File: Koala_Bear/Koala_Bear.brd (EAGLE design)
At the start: 59.3 x 40 mm, 27 parts

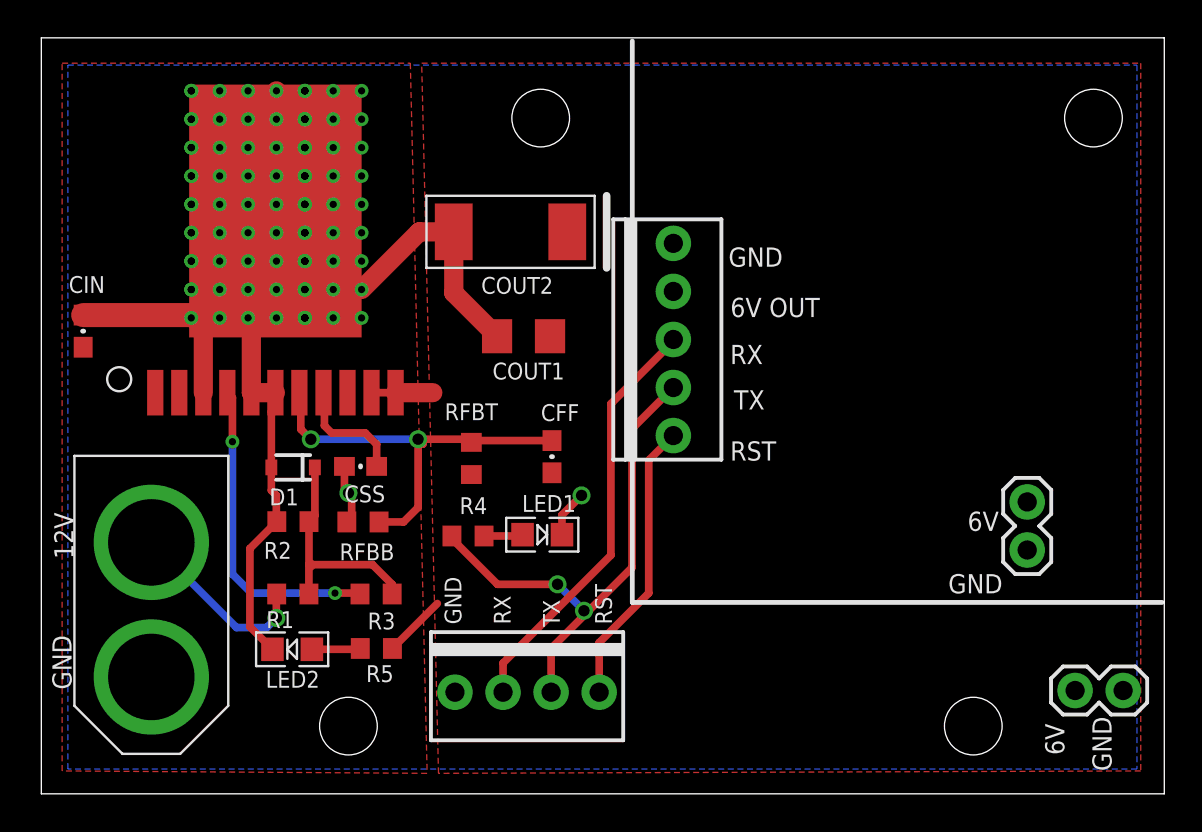
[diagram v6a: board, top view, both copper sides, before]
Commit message: Preliminary Rev C Koala
The only things that have changed since Rev B are power pin alignments
(lower right hand side), silkscreens, and power connector (the board has
now been Anderson-ified.) No changes have been made to the faulty TX LED
system; pending @douglashutchings et. al.s' go-ahead, I'll try a new fix
on that. I just wanted to get a pull request issued before the deadline.
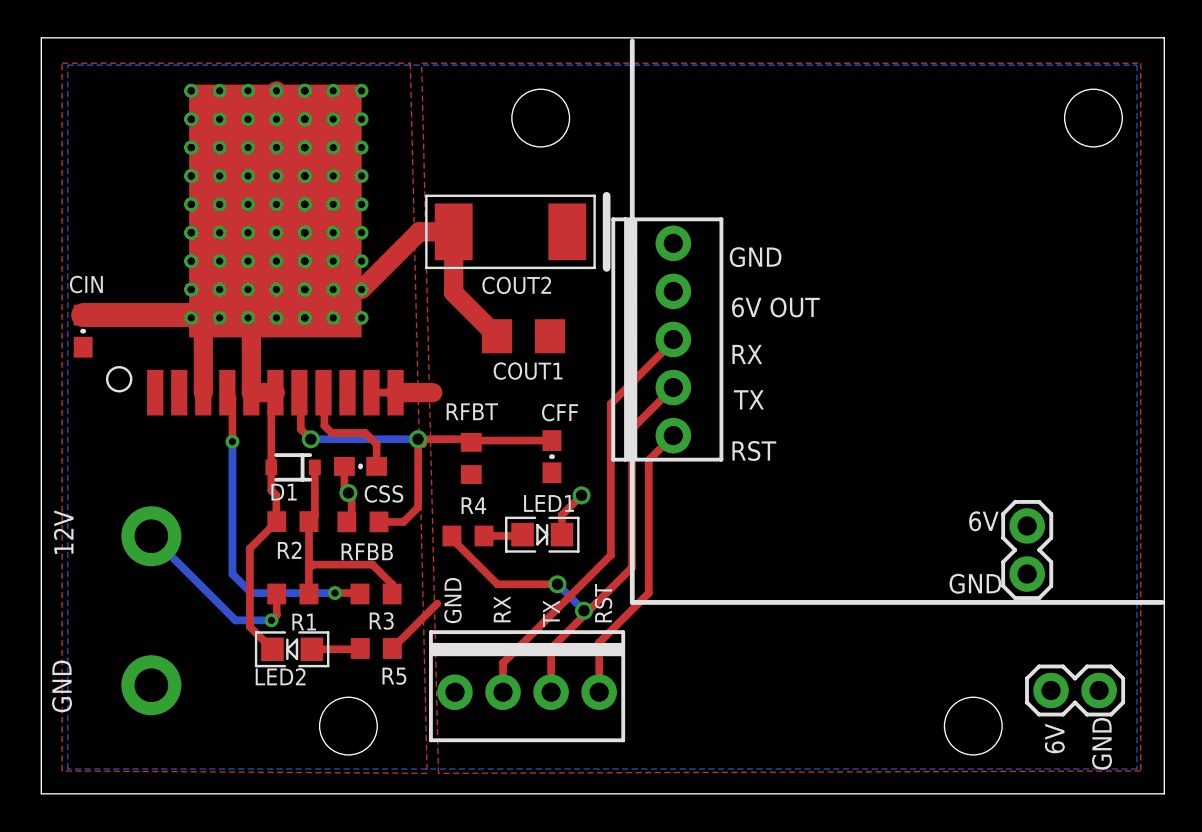
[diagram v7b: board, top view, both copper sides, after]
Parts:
- removed XT60: XT60CONNECTOR, pie_new:XT60CONNECTOR
- added U$6: ANDERSONVERTICAL, pie:ANDERSON_VERTICAL
- moved SERVO_PWR_6 1.27 mm to (60.0, 15.3)
- moved SERVO_PWR_12 1.27 mm to (62.5, 7.85)
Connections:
- net GND: now also U$6.PIN1; no longer XT60.GND
- net VIN: now also U$6.PIN2; no longer XT60.12V
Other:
- board text added: "Copyright (c) 2013, Pioneers in Engineering All rights reserved. Designed by: K. Rakelly and A. Hild This design is open source hardware. 12/21/2013"
- board text added: "PiE Robotics Buck Switching Regulator Version 2 : Revision C"
- board text removed: "Copyright (c) 2013, Pioneers in Engineering All rights reserved. Designed by: K. Rakelly and A. Hild This design is open source hardware. 11/13/2013"
- board text removed: "PiE Robotics Buck Switching Regulator Version 2 : Revision B"
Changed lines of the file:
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@@
 <setting verticaltext="up"/>
 </settings>
-<grid distance="0.005" unitdist="inch" unit="inch" style="lines" multiple="1" display="yes" altdistance="0.005" altunitdist="inch" altunit="inch"/>
+<grid distance="0.005" unitdist="inch" unit="inch" style="lines" multiple="1" display="yes" altdistance="0.1" altunitdist="inch" altunit="inch"/>
 <layers>
 <layer number="1" name="Top" color="4" fill="1" visible="yes" active="yes"/>
@@
 <layer number="97" name="Info" color="7" fill="1" visible="no" active="no"/>
 <layer number="98" name="Guide" color="6" fill="1" visible="no" active="no"/>
+<layer number="99" name="SpiceOrder" color="5" fill="1" visible="no" active="no"/>
 <layer number="100" name="Muster" color="7" fill="1" visible="no" active="no"/>
 <layer number="101" name="Patch_Top" color="12" fill="4" visible="no" active="yes"/>
@@
 <text x="57.758" y="19.658" size="1.016" layer="22" font="vector" ratio="15" rot="MR90">PiE Robotics
 Buck Switching Regulator
-Version 2 : Revision B</text>
+Version 2 : Revision C</text>
 <wire x1="67.244" y1="2.39" x2="7.9" y2="2.39" width="0" layer="20"/>
 <wire x1="39.13" y1="12.505" x2="39.13" y2="42.17291875" width="0.254" layer="25"/>
@@
 <text x="35.3" y="11.219" size="0.889" layer="21" font="vector" ratio="20" rot="R90">TX</text>
 <text x="32.7" y="11.346" size="0.889" layer="21" font="vector" ratio="20" rot="R90">RX</text>
-<text x="9.5" y="7.9" size="1.016" layer="21" font="vector" ratio="20" rot="R90">GND</text>
-<text x="9.6" y="14.8" size="1.016" layer="21" font="vector" ratio="20" rot="R90">12V</text>
+<text x="9.5" y="6.63" size="1.016" layer="21" font="vector" ratio="20" rot="R90">GND</text>
+<text x="9.6" y="14.927" size="1.016" layer="21" font="vector" ratio="20" rot="R90">12V</text>
 <text x="58.7" y="14" size="1.016" layer="21" font="vector" ratio="20" rot="R180">GND</text>
 <text x="58.5" y="17.3" size="1.016" layer="21" font="vector" ratio="20" rot="R180">6V</text>
@@
 Designed by: K. Rakelly and A. Hild
 This design is open source hardware.
-11/13/2013</text>
+12/21/2013</text>
 <text x="12.889" y="3.873" size="1.016" layer="22" font="vector" ratio="15" rot="MR180">For more information, visit pioneers.berkeley.edu/opensource</text>
 <text x="19.304" y="11.938" size="0.889" layer="27" font="vector" ratio="20" rot="R90">60k</text>
@@
 <element name="U$1" library="LMZ12010" package="LMZ12010" value="LMZ12010" x="20.27" y="33.19" smashed="yes"/>
 <element name="R1" library="pie" package="R0603" value="60k" x="21.19" y="12.95" smashed="yes" rot="R180">
-<attribute name="NAME" x="21.249359375" y="12.039359375" size="0.889" layer="25" font="vector" ratio="20" rot="R180"/>
+<attribute name="NAME" x="22.519359375" y="11.912359375" size="0.889" layer="25" font="vector" ratio="20" rot="R180"/>
 </element>
 <element name="R2" library="pie" package="R0603" value="30k" x="21.195" y="16.775" smashed="yes">
-<attribute name="NAME" x="19.66" y="14.81" size="0.889" layer="25" font="vector" ratio="20"/>
+<attribute name="NAME" x="20.295" y="14.81" size="0.889" layer="25" font="vector" ratio="20"/>
 </element>
 <element name="RFBT" library="pie" package="R0603" value="15.4k" x="30.625725" y="20.1126875" smashed="yes" rot="R270">
@@
 </element>
 <element name="CSS" library="pie" package="0603-CAP" value=".47uF" x="24.77" y="19.693" smashed="yes" rot="R180">
-<attribute name="NAME" x="26.07" y="18.683" size="0.889" layer="25" font="vector" ratio="20" rot="R180"/>
+<attribute name="NAME" x="27.086" y="18.683" size="0.889" layer="25" font="vector" ratio="20" rot="R180"/>
 </element>
 <element name="CIN" library="pie" package="0603-CAP" value="10uF" x="10.11" y="26.84" smashed="yes" rot="R90">
@@
 </element>
 <element name="D1" library="SparkFun" package="SOD-323" value="5.1V" x="21.207" y="19.64" smashed="yes" rot="R180">
-<attribute name="NAME" x="21.496" y="18.524" size="0.889" layer="25" font="vector" ratio="20" rot="R180"/>
+<attribute name="NAME" x="21.496" y="18.778" size="0.889" layer="25" font="vector" ratio="20" rot="R180"/>
 </element>
 <element name="COUT2" library="TANT_CASE_E" package="TANT_CASE_E" value="470uF" x="32.694659375" y="32.088403125" smashed="yes" rot="R180">
@@
 <attribute name="VALUE" x="32.3" y="3.315" size="1.27" layer="27"/>
 <attribute name="PARTNUMBER" value="A1922-ND" x="33.57" y="7.76" size="1.778" layer="27" display="off"/>
-</element>
-<element name="XT60" library="pie_new" package="XT60CONNECTOR" value="XT60CONNECTOR" x="9.65" y="20.25" rot="R270">
-<attribute name="PARTNUMBER" value="PRT-10474 " x="9.65" y="20.25" size="1.778" layer="27" rot="R270" display="off"/>
 </element>
 <element name="U$3" library="pie" package="STAND-OFF-TIGHT" value="" x="57.15" y="5.969"/>
@@
 <attribute name="PARTNUMBER" value="A19471-ND" x="41.3" y="26.4" size="1.778" layer="27" rot="R90" display="off"/>
 </element>
-<element name="SERVO_PWR_6" library="pie" package="1X02" value="" x="60" y="16.545" smashed="yes" rot="R270">
-<attribute name="VALUE" x="55.555" y="17.815" size="1.27" layer="27" rot="R270"/>
-</element>
-<element name="SERVO_PWR_12" library="pie" package="1X02" value="" x="63.8" y="7.85" smashed="yes" rot="R180">
-<attribute name="VALUE" x="65.07" y="11.025" size="1.27" layer="27" rot="R180"/>
+<element name="SERVO_PWR_6" library="pie" package="1X02" value="" x="60" y="15.275" smashed="yes" rot="R270">
+<attribute name="VALUE" x="55.555" y="16.545" size="1.27" layer="27" rot="R270"/>
+</element>
+<element name="SERVO_PWR_12" library="pie" package="1X02" value="" x="62.53" y="7.85" smashed="yes" rot="R180">
+<attribute name="VALUE" x="63.8" y="11.025" size="1.27" layer="27" rot="R180"/>
 </element>
 <element name="U$10" library="pie_new" package="PIE-LOGO-SMALL" value="" x="33" y="31" rot="MR270"/>
@@
 </element>
 <element name="R5" library="pie" package="R0603" value="330" x="25.604290625" y="10.071421875" smashed="yes">
-<attribute name="NAME" x="25.060475" y="8.29774375" size="0.889" layer="25" font="vector" ratio="20"/>
+<attribute name="NAME" x="25.822475" y="8.17074375" size="0.889" layer="25" font="vector" ratio="20"/>
 <attribute name="VALUE" x="28.155578125" y="8.840290625" size="0.889" layer="27" font="vector" ratio="20" rot="R90"/>
 </element>
@@
 </element>
 <element name="LED2" library="pie" package="LED-0805" value="YEL" x="21.15546875" y="10.028240625" smashed="yes" rot="R180">
-<attribute name="NAME" x="19.75846875" y="7.996240625" size="0.889" layer="25" font="vector" ratio="20"/>
+<attribute name="NAME" x="19.12346875" y="8.123240625" size="0.889" layer="25" font="vector" ratio="20"/>
 <attribute name="VALUE" x="17.98046875" y="11.298240625" size="0.889" layer="27" font="vector" ratio="20" rot="R270"/>
 </element>
 <element name="U$2" library="pie" package="STAND-OFF-TIGHT" value="" x="63.5" y="38.1"/>
+<element name="U$6" library="pie" package="ANDERSON_VERTICAL" value="ANDERSONVERTICAL" x="13.716" y="12.065" smashed="yes">
+<attribute name="PARTNUMBER" value="1377G3" x="13.716" y="12.065" size="1.778" layer="27" display="off"/>
+</element>
 </elements>
 <signals>
@@
 <contactref element="SERVO_PWR_12" pad="1"/>
 <contactref element="MSTRO_PWR" pad="5"/>
-<contactref element="XT60" pad="GND"/>
 <wire x1="16.46" y1="23.5888" x2="16.46" y2="27.56" width="1.016" layer="1"/>
 <wire x1="16.46" y1="27.56" x2="16.95" y2="28.05" width="1.016" layer="1"/>
@@
 <wire x1="31.984553125" y1="26.572975" x2="29.694659375" y2="28.86286875" width="1.016" layer="1"/>
 <wire x1="29.694659375" y1="28.86286875" x2="29.694659375" y2="32.088403125" width="1.016" layer="1"/>
+<contactref element="U$6" pad="PIN1"/>
 </signal>
 <signal name="VOUT">
@@
 <contactref element="CIN" pad="1"/>
 <contactref element="R1" pad="2"/>
-<contactref element="XT60" pad="12V"/>
 <polygon width="0.4064" layer="1">
 <vertex x="9" y="41"/>
@@
 <vertex x="9" y="3.6"/>
 </polygon>
-<wire x1="20.34" y1="12.95" x2="20.32" y2="12.95" width="0.4064" layer="1"/>
-<wire x1="20.32" y1="12.95" x2="20.32" y2="11.684" width="0.4064" layer="1"/>
-<via x="20.32" y="11.684" extent="1-16" drill="0.6"/>
-<wire x1="13.714" y1="15.678" x2="18.216" y2="11.176" width="0.4064" layer="16"/>
-<wire x1="18.216" y1="11.176" x2="19.812" y2="11.176" width="0.4064" layer="16"/>
-<wire x1="19.812" y1="11.176" x2="20.32" y2="11.684" width="0.4064" layer="16"/>
+<contactref element="U$6" pad="PIN2"/>
+<wire x1="20.34" y1="12.95" x2="20.34" y2="11.831" width="0.4064" layer="1"/>
+<wire x1="20.34" y1="11.831" x2="20.066" y2="11.557" width="0.4064" layer="1"/>
+<wire x1="13.716" y1="16.002" x2="18.161" y2="11.557" width="0.4064" layer="16"/>
+<wire x1="18.161" y1="11.557" x2="20.066" y2="11.557" width="0.4064" layer="16"/>
+<via x="20.066" y="11.557" extent="1-16" drill="0.381" diameter="0.7366"/>
 </signal>
 <signal name="FB">

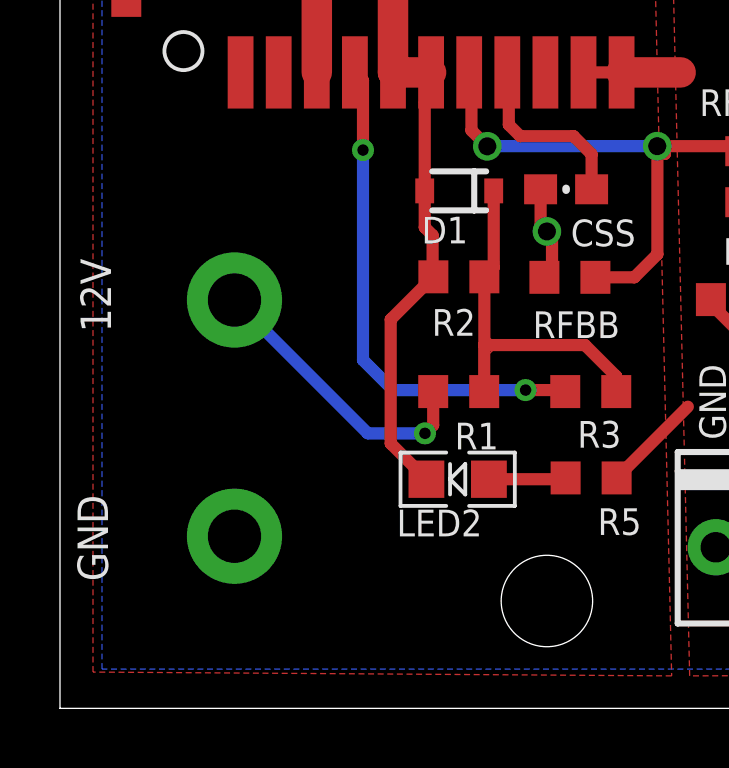
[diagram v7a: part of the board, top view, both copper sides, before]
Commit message: Response to review
Anderson connector now divested of >NAME silkscreen (thanks for fixing
the part! I updated my repo and it worked like a charm from there.)

Increased width of trace coming from 12V pin to 0.027", which seemed to
be the result yielded by PiE's trace width calculator. Thoughts?
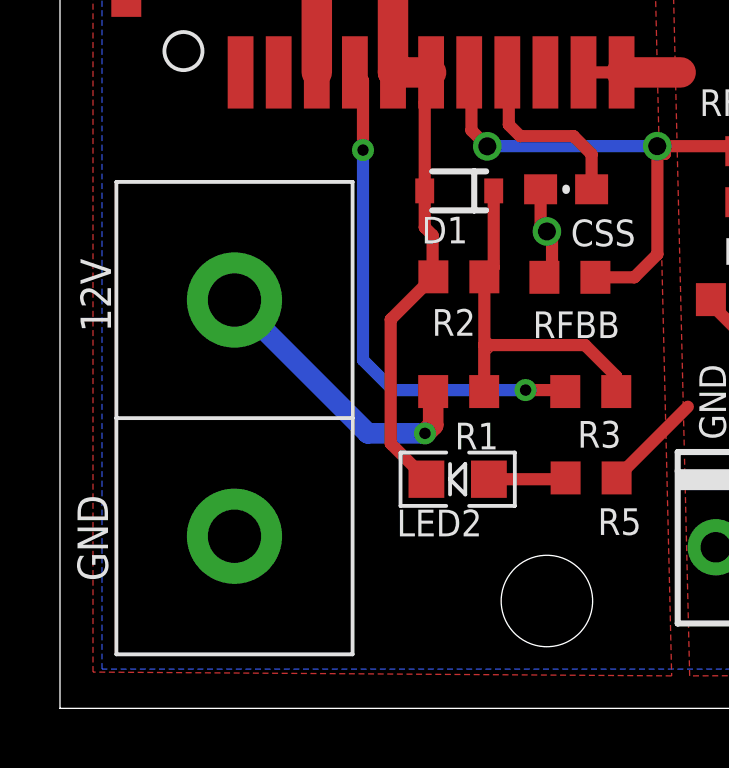
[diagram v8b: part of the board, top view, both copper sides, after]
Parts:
- renumbered U$6 to PWR
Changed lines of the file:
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@@
 </element>
 <element name="U$2" library="pie" package="STAND-OFF-TIGHT" value="" x="63.5" y="38.1"/>
-<element name="U$6" library="pie" package="ANDERSON_VERTICAL" value="ANDERSONVERTICAL" x="13.716" y="12.065" smashed="yes">
+<element name="PWR" library="pie" package="ANDERSON_VERTICAL" value="ANDERSONVERTICAL" x="13.716" y="12.065" smashed="yes">
 <attribute name="PARTNUMBER" value="1377G3" x="13.716" y="12.065" size="1.778" layer="27" display="off"/>
 </element>
@@
 <wire x1="31.984553125" y1="26.572975" x2="29.694659375" y2="28.86286875" width="1.016" layer="1"/>
 <wire x1="29.694659375" y1="28.86286875" x2="29.694659375" y2="32.088403125" width="1.016" layer="1"/>
-<contactref element="U$6" pad="PIN1"/>
+<contactref element="PWR" pad="PIN1"/>
 </signal>
 <signal name="VOUT">
@@
 <vertex x="9" y="3.6"/>
 </polygon>
-<contactref element="U$6" pad="PIN2"/>
-<wire x1="20.34" y1="12.95" x2="20.34" y2="11.831" width="0.4064" layer="1"/>
-<wire x1="20.34" y1="11.831" x2="20.066" y2="11.557" width="0.4064" layer="1"/>
-<wire x1="13.716" y1="16.002" x2="18.161" y2="11.557" width="0.4064" layer="16"/>
-<wire x1="18.161" y1="11.557" x2="20.066" y2="11.557" width="0.4064" layer="16"/>
+<contactref element="PWR" pad="PIN2"/>
+<wire x1="20.34" y1="12.95" x2="20.34" y2="11.831" width="0.6858" layer="1"/>
+<wire x1="20.34" y1="11.831" x2="20.066" y2="11.557" width="0.6858" layer="1"/>
+<wire x1="13.716" y1="16.002" x2="18.161" y2="11.557" width="0.6858" layer="16"/>
+<wire x1="18.161" y1="11.557" x2="20.066" y2="11.557" width="0.6858" layer="16"/>
 <via x="20.066" y="11.557" extent="1-16" drill="0.381" diameter="0.7366"/>
 </signal>
